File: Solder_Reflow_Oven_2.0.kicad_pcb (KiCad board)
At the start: 2 copper layers, 64.8 x 61.2 mm, 45 parts, among them J1 Conn_01x02_Male, J2 USB_B_Micro, J3 Conn_01x02_Male, J4 Conn_02x03_Top_Bottom, J5 Conn_01x02_Top_Bottom, J6 Conn_01x02_Male, J7 Conn_01x24_Male, Q1 2SD1805, SW1 SW_DIP_x01, U1 LM2940IMPX-10/NOPB, U2 MAX31855KASA, U3 RCLAMP0502A.TCT, U4 STM32L053R6T6, U5 CDBHD140L-G, U6 F24-100-C2, U7 SPDT_Reflow, Y1 Crystal_GND24

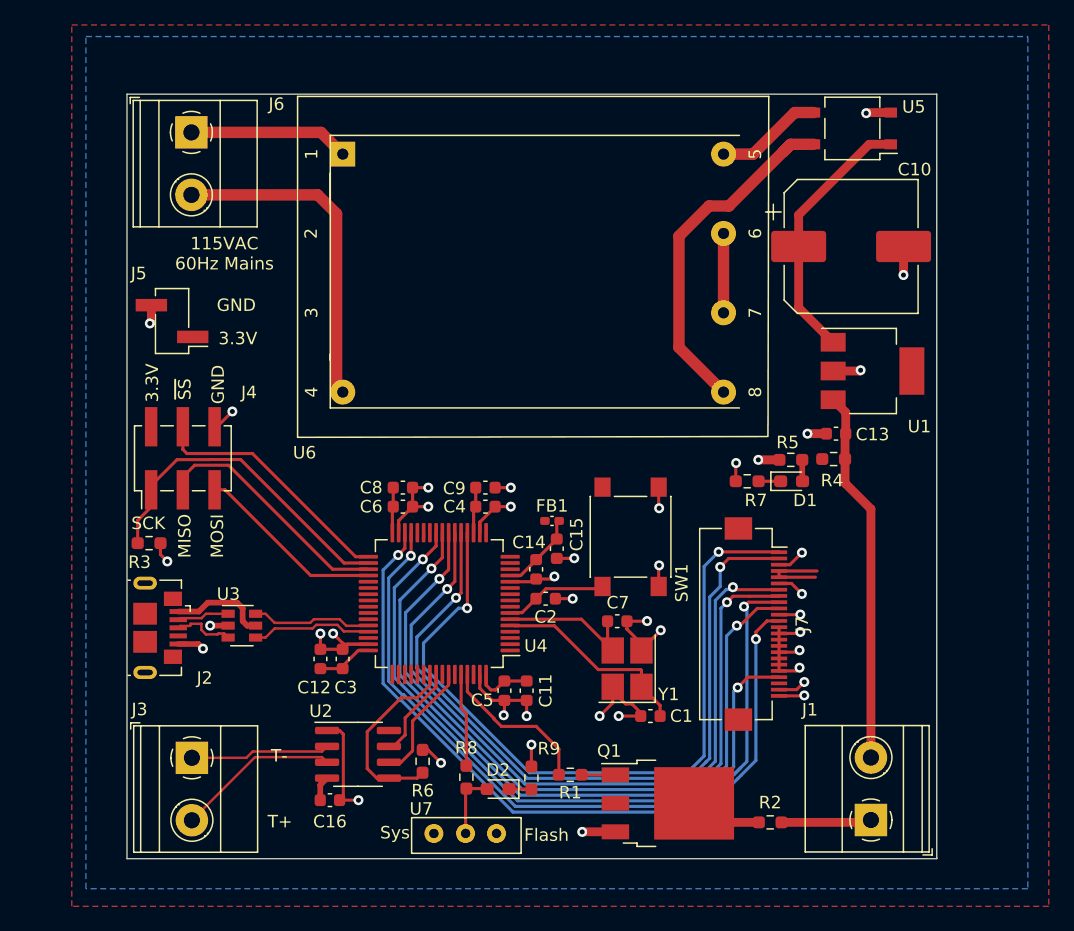
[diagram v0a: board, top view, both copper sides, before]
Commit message: Updating Design for through hole components
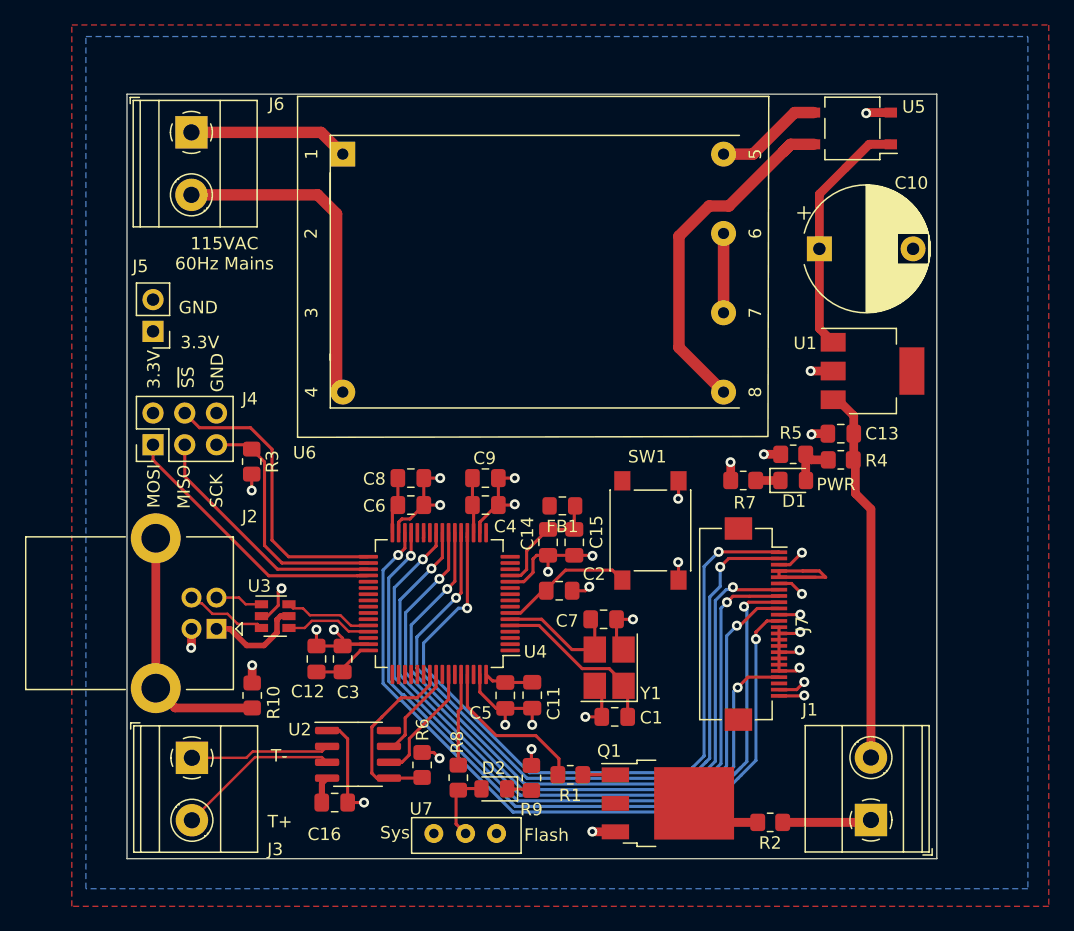
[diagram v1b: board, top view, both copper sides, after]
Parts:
- added R10: R, Resistor_SMD:R_0805_2012Metric_Pad1.20x1.40mm_HandSolder, F.Cu at (49.4, 121.8)
- C1, C11, C12, C13, C14, C15, C16, C2, C3, C4, C5, C6, C7, C8, C9: footprint Capacitor_SMD:C_0603_1608Metric -> Capacitor_SMD:C_0805_2012Metric_Pad1.18x1.45mm_HandSolder
- C10: footprint Capacitor_SMD:CP_Elec_10x14.3 -> Capacitor_THT:CP_Radial_D10.0mm_P7.50mm
- D1, D2: footprint LED_SMD:LED_0603_1608Metric_Pad1.05x0.95mm_HandSolder -> LED_SMD:LED_0805_2012Metric_Pad1.15x1.40mm_HandSolder
- FB1: footprint Inductor_SMD:L_0402_1005Metric_Pad0.77x0.64mm_HandSolder -> Inductor_SMD:L_0805_2012Metric_Pad1.15x1.40mm_HandSolder
- J2: value USB_B_Micro -> USB_B; footprint Connector_USB:USB_Micro-B_GCT_USB3076-30-A -> Connector_USB:USB_B_Lumberg_2411_02_Horizontal
- J4: footprint Connector_PinHeader_2.54mm:PinHeader_2x03_P2.54mm_Vertical_SMD -> Connector_PinHeader_2.54mm:PinHeader_2x03_P2.54mm_Vertical
- J5: footprint Connector_PinHeader_2.54mm:PinHeader_1x02_P2.54mm_Vertical_SMD_Pin1Left -> Connector_PinHeader_2.54mm:PinHeader_1x02_P2.54mm_Vertical
- R1, R2, R3, R4, R5, R6, R7, R8, R9: footprint Resistor_SMD:R_0603_1608Metric_Pad0.98x0.95mm_HandSolder -> Resistor_SMD:R_0805_2012Metric_Pad1.20x1.40mm_HandSolder
- moved R3 10.5 mm to (49.4, 103.1), turned to 270 degrees
- moved J2 4.52 mm to (46.5, 116.5), turned to 180 degrees
- moved C1 2.86 mm to (78.4, 123.5)
- moved U3 2.77 mm to (51.2, 115.4)
- moved J4 2.62 mm to (41.5, 101.7)
- moved C10 2.55 mm to (94.8, 86.0)
- moved C14 2.36 mm to (73.1, 109.5)
- moved J5 1.73 mm to (41.5, 92.6)
- moved SW1 1.67 mm to (81.3, 108.6)
- moved C15 1.49 mm to (75.2, 109.5)
- moved FB1 1.46 mm to (74.2, 106.6)
- moved Y1 1.44 mm to (78.0, 119.6)
- moved C2 1.25 mm to (74.0, 113.4)
- moved C7 1.10 mm to (77.5, 115.7)
- moved C8 0.99 mm to (62.1, 104.4)
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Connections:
- J2 pad 4: Net-(J2-Pad4) -> VSS
- J2 pad 5: VSS -> Net-(J2-Pad5)
- J4 pad 1: SPI1_SCK -> SPI1_MOSI
- J4 pad 5: SPI1_MOSI -> SPI1_SCK
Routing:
- net Net-(J2-Pad5): track 0.00 -> 20.4 mm
- net VDD_3.3: track 26.6 -> 37.8 mm
- net SPI1_MOSI: track 15.1 -> 22.2 mm
- net SPI1_SCK: track 26.7 -> 20.0 mm
- net SPI_NSS: track 20.2 -> 23.7 mm
- net VSS: track 106.8 -> 103.7 mm, vias 40 -> 36
- net VDDA_3.3: track 6.49 -> 9.50 mm
- net USBD+: track 9.67 -> 6.95 mm
- net USBD-: track 9.67 -> 7.08 mm
- net NRST: track 8.27 -> 10.8 mm
- net OSC_IN: track 16.3 -> 13.8 mm
- net USB_CONN+: track 5.00 -> 6.61 mm
- net OSC_OUT: track 11.8 -> 10.3 mm
- net Net-(C10-Pad1): track 21.1 -> 19.7 mm
- net SPI2_SCK: track 15.3 -> 14.4 mm
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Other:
- board text added: "PWR"
